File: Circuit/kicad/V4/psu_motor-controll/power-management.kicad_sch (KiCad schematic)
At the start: 2 parts, among them J4 SERVO_VOLTAGE_SELECT

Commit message: kicad psu pcb finish psu
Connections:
- net +5V: now also J4.5 (Pin_5); no longer J4.2 (Pin_2)
- net +6V: now also J4.2 (Pin_2); no longer J4.5 (Pin_5)

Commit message: V4.1.7 PSU  V1.0 debug Card
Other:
- removed sheet diagram
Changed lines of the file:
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@@
 	(wire
 		(pts
-			(xy 83.82 54.61) (xy 91.44 54.61)
+			(xy 50.8 54.61) (xy 91.44 54.61)
 		)
 		(stroke
@@
 	(wire
 		(pts
-			(xy 83.82 52.07) (xy 91.44 52.07)
+			(xy 50.8 52.07) (xy 91.44 52.07)
 		)
 		(stroke
@@
 	)
 	(label "SW_N"
-		(at 83.82 52.07 0)
+		(at 50.8 52.07 0)
 		(effects
 			(font
@@
 	)
 	(label "SW_P"
-		(at 83.82 54.61 0)
+		(at 50.8 54.61 0)
 		(effects
 			(font
@@
 				)
 			)
-		)
-	)
-	(sheet
-		(at 17.78 19.05)
-		(size 12.7 3.81)
-		(exclude_from_sim no)
-		(in_bom yes)
-		(on_board yes)
-		(dnp no)
-		(fields_autoplaced yes)
-		(stroke
-			(width 0.1524)
-			(type solid)
-		)
-		(fill
-			(color 0 0 0 0.0000)
-		)
-		(property "Sheetname" "diagram"
-			(at 17.78 18.3384 0)
-			(effects
-				(font
-					(size 1.27 1.27)
-				)
-				(justify left bottom)
-			)
-		)
-		(property "Sheetfile" "diagram.kicad_sch"
-			(at 17.78 23.4446 0)
-			(effects
-				(font
-					(size 1.27 1.27)
-				)
-				(justify left top)
-			)
-		)
-		(instances
-			(project "psu"
-				(path "/e63e39d7-6ac0-4ffd-8aa3-1841a4541b55/4c1824a3-ede3-44a9-9cc4-1658cb86e3ae"
-					(page "11")
-				)
-			)

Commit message: updated bom, updated compon
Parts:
- DSW1: Cikkszám (none) -> 100.220.12; Link (none) -> https://www.hestore.hu/prod_10022012.html
- J4: Cikkszám (none) -> 100.387.12; Link (none) -> https://www.hestore.hu/prod_10038712.html
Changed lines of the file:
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@@
 			)
 		)
-		(property "Datasheet" "~"
+		(property "Datasheet" "https://www.hestore.hu/prod_getfile.php?id=10186"
 			(at 102.87 67.31 0)
 			(effects
@@
 		)
 		(property "Description" "Generic connector, double row, 02x03, odd/even pin numbering scheme (row 1 odd numbers, row 2 even numbers), script generated (kicad-library-utils/schlib/autogen/connector/)"
+			(at 102.87 67.31 0)
+			(effects
+				(font
+					(size 1.27 1.27)
+				)
+				(hide yes)
+			)
+		)
+		(property "Cikkszám" "100.387.12"
+			(at 102.87 67.31 0)
+			(effects
+				(font
+					(size 1.27 1.27)
+				)
+				(hide yes)
+			)
+		)
+		(property "Link" "https://www.hestore.hu/prod_10038712.html"
 			(at 102.87 67.31 0)
 			(effects
@@
 			)
 		)
-		(property "Sim.Device" ""
+		(property "Cikkszám" "100.220.12"
 			(at 62.23 116.84 0)
 			(effects
@@
 			)
 		)
-		(property "Sim.Type" ""
+		(property "Link" "https://www.hestore.hu/prod_10022012.html"
 			(at 62.23 116.84 0)
 			(effects

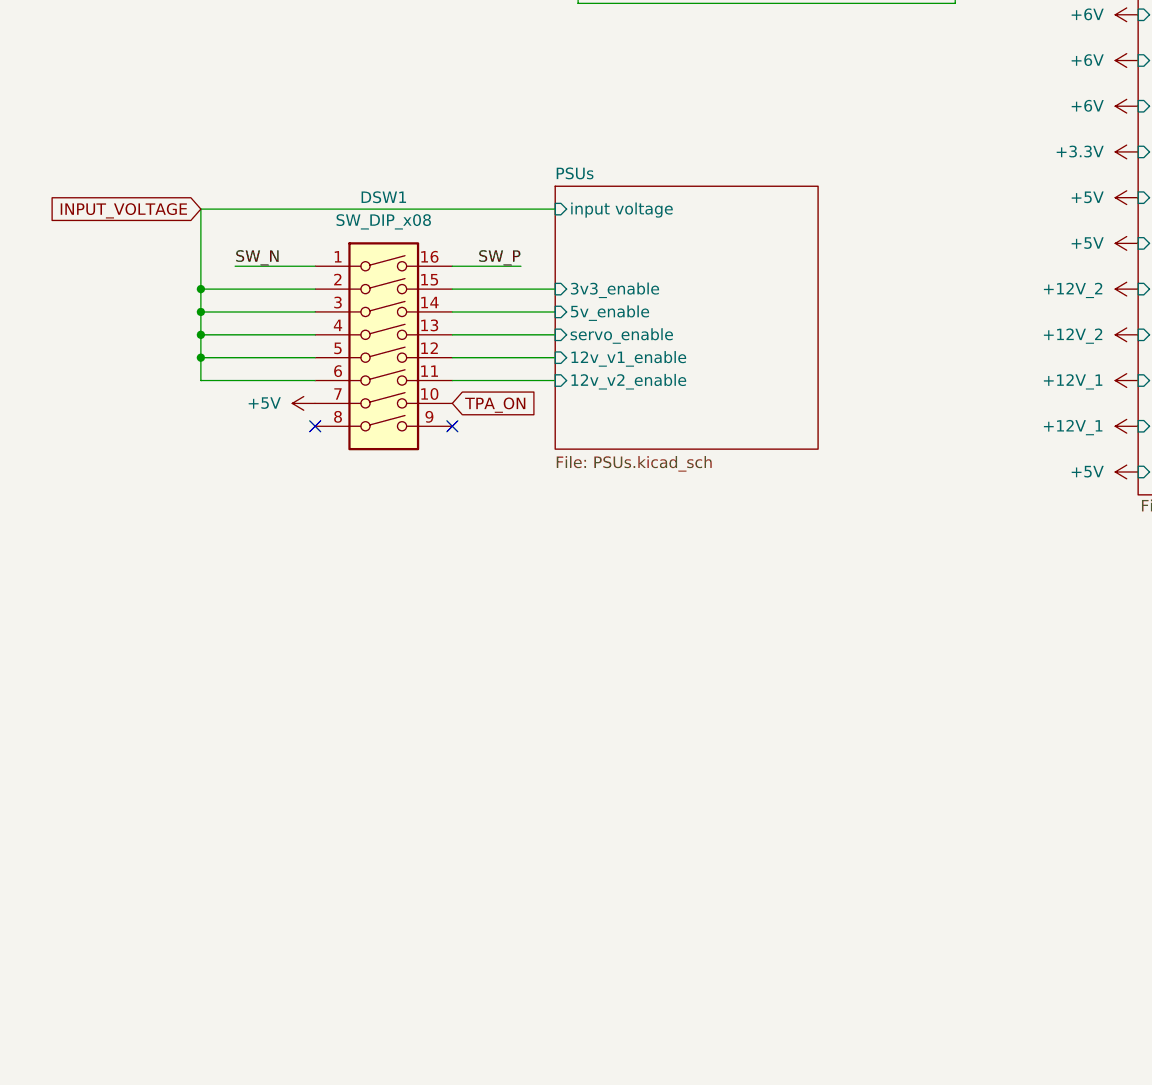
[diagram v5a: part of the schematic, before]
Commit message: added psu start delay rc tag, high speed first inner and outboard impedance calculations
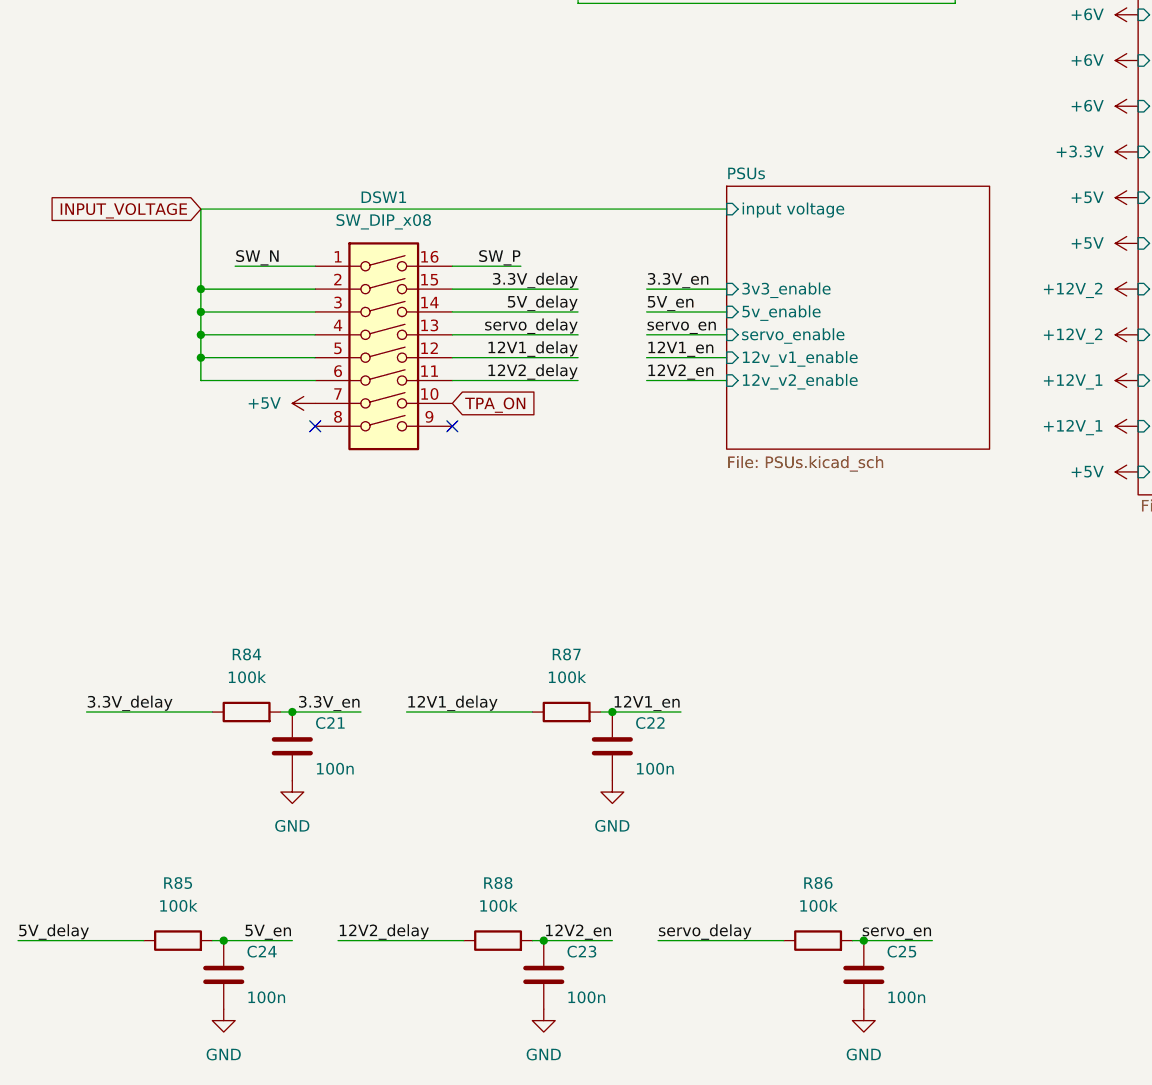
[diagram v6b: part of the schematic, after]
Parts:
- added C21, C22, C23, C24, C25: 100n, Capacitor_SMD:C_0805_2012Metric, symbol Device:C
- added R84, R85, R86, R87, R88: 100k, Resistor_SMD:R_0805_2012Metric, symbol Device:R
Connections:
- net PSUs/12v_v1_enable renamed 12V1_delay
- net 12V1_delay: now also R87.1
- net PSUs/12v_v2_enable renamed 12V2_delay
- net 12V2_delay: now also R88.1
- net PSUs/3v3_enable renamed 3.3V_delay
- net 3.3V_delay: now also R84.1
- net PSUs/5v_enable renamed 5V_delay
- net 5V_delay: now also R85.1
- net PSUs/servo_enable renamed servo_delay
- net servo_delay: now also R86.1
- new net 12V1_en: C22.1, R87.2
- new net 12V2_en: C23.1, R88.2
- new net 3.3V_en: C21.1, R84.2
- new net 5V_en: C24.1, R85.2
- new net GND: C21.2, C22.2, C23.2, C24.2, C25.2
- new net servo_en: C25.1, R86.2
